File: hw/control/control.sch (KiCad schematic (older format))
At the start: 3 parts, among them J101 Screw_Terminal_01x02, J102 Screw_Terminal_01x03, J103 Screw_Terminal_01x03

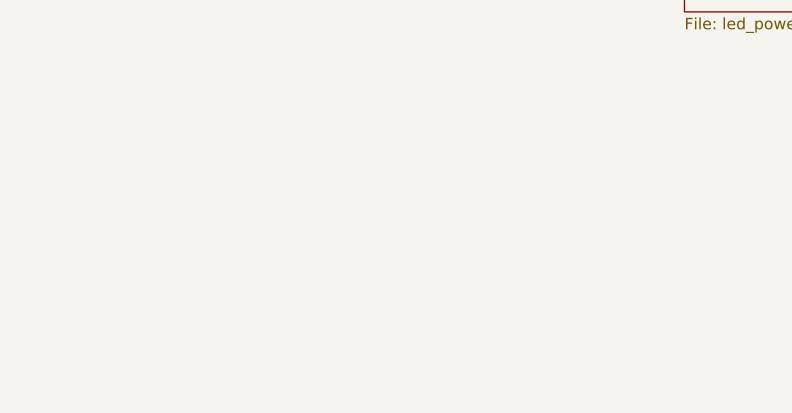
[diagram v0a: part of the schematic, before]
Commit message: [hw] Spread-out the components on control layout
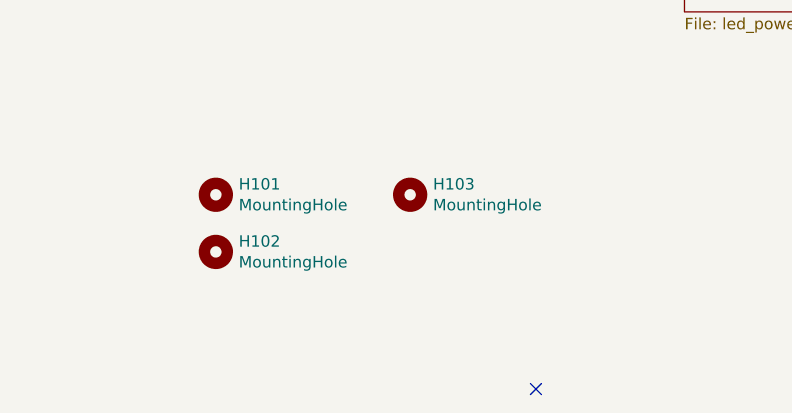
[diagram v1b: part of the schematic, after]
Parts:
- added H101, H102, H103: MountingHole, MountingHole:MountingHole_2.7mm_M2.5, symbol Mechanical:MountingHole
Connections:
- no-connect marks 0 -> 1
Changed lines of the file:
@@
 Wire Wire Line
 	3300 2550 3100 2550
+NoConn ~ 3200 7250
 Wire Bus Line
 	6350 3000 6350 4750
@@
 Wire Bus Line
 	6250 2750 6250 5050
+$Comp
+L Mechanical:MountingHole H101
+U 1 1 6167B012
+P 1800 6400
+F 0 "H101" H 1900 6446 50  0000 L CNN
+F 1 "MountingHole" H 1900 6355 50  0000 L CNN
+F 2 "MountingHole:MountingHole_2.7mm_M2.5" H 1800 6400 50  0001 C CNN
+F 3 "~" H 1800 6400 50  0001 C CNN
+	1    1800 6400
+	1    0    0    -1
+$EndComp
+$Comp
+L Mechanical:MountingHole H102
+U 1 1 6167B2FA
+P 1800 6650
+F 0 "H102" H 1900 6696 50  0000 L CNN
+F 1 "MountingHole" H 1900 6605 50  0000 L CNN
+F 2 "MountingHole:MountingHole_2.7mm_M2.5" H 1800 6650 50  0001 C CNN
+F 3 "~" H 1800 6650 50  0001 C CNN
+	1    1800 6650
+	1    0    0    -1
+$EndComp
+$Comp
+L Mechanical:MountingHole H103
+U 1 1 6167B527
+P 2650 6400
+F 0 "H103" H 2750 6446 50  0000 L CNN
+F 1 "MountingHole" H 2750 6355 50  0000 L CNN
+F 2 "MountingHole:MountingHole_2.7mm_M2.5" H 2650 6400 50  0001 C CNN
+F 3 "~" H 2650 6400 50  0001 C CNN
+	1    2650 6400
+	1    0    0    -1
+$EndComp
 $EndSCHEMATC

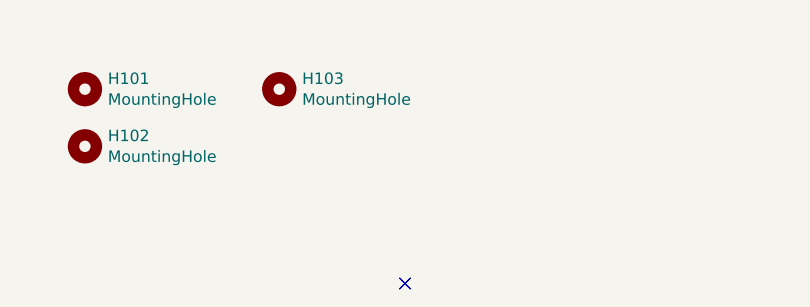
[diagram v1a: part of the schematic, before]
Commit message: [hw] Add control board net classes
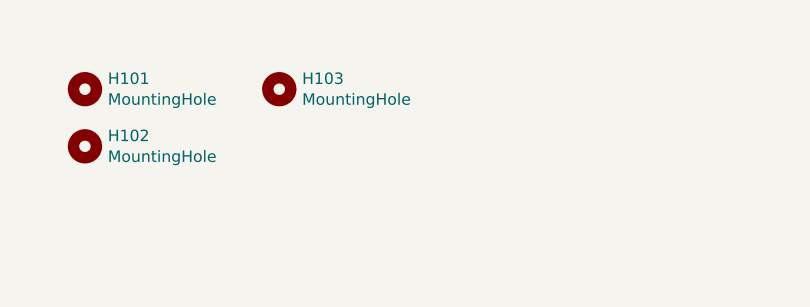
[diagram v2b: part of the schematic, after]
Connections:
- no-connect marks 1 -> 0
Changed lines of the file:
@@
 Wire Wire Line
 	3300 2550 3100 2550
-NoConn ~ 3200 7250
-Wire Bus Line
-	6350 3000 6350 4750
-Wire Bus Line
-	5950 2500 5950 5500
-Wire Bus Line
-	6250 2750 6250 5050
 $Comp
 L Mechanical:MountingHole H101
@@
 	1    0    0    -1
 $EndComp
+Wire Bus Line
+	6350 3000 6350 4750
+Wire Bus Line
+	5950 2500 5950 5500
+Wire Bus Line
+	6250 2750 6250 5050
 $EndSCHEMATC

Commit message: [hw] Incorporate suggestions
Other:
- moved on the sheet: J101, J103
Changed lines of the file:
@@
 L Connector:Screw_Terminal_01x03 J103
 U 1 1 614B768A
-P 9200 5100
-F 0 "J103" H 9350 5050 50  0000 C CNN
-F 1 "Screw_Terminal_01x03" H 9700 5200 50  0000 C CNN
-F 2 "TerminalBlock_Phoenix:TerminalBlock_Phoenix_MKDS-1,5-3_1x03_P5.00mm_Horizontal" H 9200 5100 50  0001 C CNN
-F 3 "~" H 9200 5100 50  0001 C CNN
-	1    9200 5100
-	1    0    0    1
+P 9200 5300
+F 0 "J103" H 9350 5250 50  0000 C CNN
+F 1 "Screw_Terminal_01x03" H 9700 5400 50  0000 C CNN
+F 2 "TerminalBlock_Phoenix:TerminalBlock_Phoenix_MKDS-1,5-3_1x03_P5.00mm_Horizontal" H 9200 5300 50  0001 C CNN
+F 3 "~" H 9200 5300 50  0001 C CNN
+	1    9200 5300
+	1    0    0    -1
 $EndComp
 $Comp
 L power:GND #PWR0103
 U 1 1 614C271E
-P 9650 4750
-F 0 "#PWR0103" H 9650 4500 50  0001 C CNN
-F 1 "GND" H 9655 4577 50  0000 C CNN
-F 2 "" H 9650 4750 50  0001 C CNN
-F 3 "" H 9650 4750 50  0001 C CNN
-	1    9650 4750
+P 9000 4600
+F 0 "#PWR0103" H 9000 4350 50  0001 C CNN
+F 1 "GND" H 9005 4427 50  0000 C CNN
+F 2 "" H 9000 4600 50  0001 C CNN
+F 3 "" H 9000 4600 50  0001 C CNN
+	1    9000 4600
 	1    0    0    -1
 $EndComp
@@
 Wire Wire Line
 	3650 3350 3650 2550
-Wire Wire Line
-	3650 2550 3300 2550
 Connection ~ 3650 3350
 Entry Wire Line
@@
 	5850 5450 5200 5450
 Wire Wire Line
-	9650 4750 9000 4750
-Wire Wire Line
-	9000 4750 9000 4500
-Wire Wire Line
-	9000 4750 9000 5000
-Connection ~ 9000 4750
+	9000 4600 9000 4500
 Wire Wire Line
 	8600 4650 8800 4650
@@
 	8600 4850 8800 4850
 Wire Wire Line
-	8800 4850 8800 5100
-Wire Wire Line
-	8800 5100 9000 5100
+	8800 4850 8800 5300
+Wire Wire Line
+	8800 5300 9000 5300
 Wire Wire Line
 	5200 5200 9000 5200
@@
 L Connector:Screw_Terminal_01x02 J101
 U 1 1 615338F7
-P 1350 2600
-F 0 "J101" H 1268 2817 50  0000 C CNN
-F 1 "Screw_Terminal_01x02" H 1268 2726 50  0000 C CNN
-F 2 "TerminalBlock_Phoenix:TerminalBlock_Phoenix_MKDS-1,5-2_1x02_P5.00mm_Horizontal" H 1350 2600 50  0001 C CNN
-F 3 "~" H 1350 2600 50  0001 C CNN
-	1    1350 2600
+P 1000 2600
+F 0 "J101" H 918 2817 50  0000 C CNN
+F 1 "Screw_Terminal_01x02" H 918 2726 50  0000 C CNN
+F 2 "TerminalBlock_Phoenix:TerminalBlock_Phoenix_MKDS-1,5-2_1x02_P5.00mm_Horizontal" H 1000 2600 50  0001 C CNN
+F 3 "~" H 1000 2600 50  0001 C CNN
+	1    1000 2600
 	-1   0    0    -1
 $EndComp
 Wire Wire Line
-	1650 2550 1650 2600
-Wire Wire Line
-	1650 2600 1550 2600
-Wire Wire Line
-	1650 2750 1650 2700
-Wire Wire Line
-	1650 2700 1550 2700
+	1450 2550 1450 2600
+Wire Wire Line
+	1450 2600 1200 2600
+Wire Wire Line
+	1450 2750 1450 2700
+Wire Wire Line
+	1450 2700 1200 2700
 Wire Wire Line
 	5650 3350 5650 3200
@@
 P 5400 3350
 F 0 "#FLG0103" H 5400 3425 50  0001 C CNN
-F 1 "PWR_FLAG" H 5400 3523 50  0000 C CNN
+F 1 "PWR_FLAG" H 5400 3500 50  0000 C CNN
 F 2 "" H 5400 3350 50  0001 C CNN
 F 3 "~" H 5400 3350 50  0001 C CNN
@@
 Wire Wire Line
 	5400 3350 5650 3350
-$Comp
-L power:PWR_FLAG #FLG0102
-U 1 1 61668437
-P 3300 2750
-F 0 "#FLG0102" H 3300 2825 50  0001 C CNN
-F 1 "PWR_FLAG" H 3300 2900 50  0000 C CNN
-F 2 "" H 3300 2750 50  0001 C CNN
-F 3 "~" H 3300 2750 50  0001 C CNN
-	1    3300 2750
-	1    0    0    -1
-$EndComp
-Connection ~ 3300 2750
-Wire Wire Line
-	1650 2750 2000 2750
-Wire Wire Line
-	1650 2550 2000 2550
-$Comp
-L power:PWR_FLAG #FLG0101
-U 1 1 6166B01E
-P 3300 2550
-F 0 "#FLG0101" H 3300 2625 50  0001 C CNN
-F 1 "PWR_FLAG" H 3300 2723 50  0000 C CNN
-F 2 "" H 3300 2550 50  0001 C CNN
-F 3 "~" H 3300 2550 50  0001 C CNN
-	1    3300 2550
-	1    0    0    -1
-$EndComp
-Connection ~ 3300 2550
-Wire Wire Line
-	3300 2550 3100 2550
+Wire Wire Line
+	1450 2750 1750 2750
+Wire Wire Line
+	1450 2550 1750 2550
 $Comp
 L Mechanical:MountingHole H101
@@
 	1    0    0    -1
 $EndComp
+$Comp
+L power:GND #PWR0104
+U 1 1 6169E8B0
+P 9000 5500
+F 0 "#PWR0104" H 9000 5250 50  0001 C CNN
+F 1 "GND" H 9005 5327 50  0000 C CNN
+F 2 "" H 9000 5500 50  0001 C CNN
+F 3 "" H 9000 5500 50  0001 C CNN
+	1    9000 5500
+	1    0    0    -1
+$EndComp
+Wire Wire Line
+	9000 5500 9000 5400
+$Comp
+L power:PWR_FLAG #FLG0101
+U 1 1 616A47D9
+P 1750 2550
+F 0 "#FLG0101" H 1750 2625 50  0001 C CNN
+F 1 "PWR_FLAG" H 1750 2700 50  0000 C CNN
+F 2 "" H 1750 2550 50  0001 C CNN
+F 3 "~" H 1750 2550 50  0001 C CNN
+	1    1750 2550
+	1    0    0    -1
+$EndComp
+Connection ~ 1750 2550
+Wire Wire Line
+	1750 2550 2000 2550
+$Comp
+L power:PWR_FLAG #FLG0102
+U 1 1 616A4B57
+P 1750 2750
+F 0 "#FLG0102" H 1750 2825 50  0001 C CNN
+F 1 "PWR_FLAG" H 1750 2900 50  0000 C CNN
+F 2 "" H 1750 2750 50  0001 C CNN
+F 3 "~" H 1750 2750 50  0001 C CNN
+	1    1750 2750
+	1    0    0    -1
+$EndComp
+Connection ~ 1750 2750
+Wire Wire Line
+	1750 2750 2000 2750
+Wire Wire Line
+	3100 2550 3500 2550
+$Comp
+L power:PWR_FLAG #FLG0104
+U 1 1 616A5315
+P 3500 2550
+F 0 "#FLG0104" H 3500 2625 50  0001 C CNN
+F 1 "PWR_FLAG" H 3500 2700 50  0000 C CNN
+F 2 "" H 3500 2550 50  0001 C CNN
+F 3 "~" H 3500 2550 50  0001 C CNN
+	1    3500 2550
+	1    0    0    -1
+$EndComp
+Connection ~ 3500 2550
+Wire Wire Line
+	3500 2550 3650 2550
 Wire Bus Line
 	6350 3000 6350 4750

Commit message: [hw] Re-annotate all components
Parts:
- renumbered H103 to H102, H102 to H103
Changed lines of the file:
@@
 LED_DATA_~EN~1
 $Comp
-L power:PWR_FLAG #FLG0103
+L power:PWR_FLAG #FLG0104
 U 1 1 61664238
 P 5400 3350
-F 0 "#FLG0103" H 5400 3425 50  0001 C CNN
+F 0 "#FLG0104" H 5400 3425 50  0001 C CNN
 F 1 "PWR_FLAG" H 5400 3500 50  0000 C CNN
 F 2 "" H 5400 3350 50  0001 C CNN
@@
 $EndComp
 $Comp
-L Mechanical:MountingHole H102
+L Mechanical:MountingHole H103
 U 1 1 6167B2FA
 P 1800 6650
-F 0 "H102" H 1900 6696 50  0000 L CNN
+F 0 "H103" H 1900 6696 50  0000 L CNN
 F 1 "MountingHole" H 1900 6605 50  0000 L CNN
 F 2 "MountingHole:MountingHole_2.7mm_M2.5" H 1800 6650 50  0001 C CNN
@@
 $EndComp
 $Comp
-L Mechanical:MountingHole H103
+L Mechanical:MountingHole H102
 U 1 1 6167B527
 P 2650 6400
-F 0 "H103" H 2750 6446 50  0000 L CNN
+F 0 "H102" H 2750 6446 50  0000 L CNN
 F 1 "MountingHole" H 2750 6355 50  0000 L CNN
 F 2 "MountingHole:MountingHole_2.7mm_M2.5" H 2650 6400 50  0001 C CNN
@@
 	1750 2550 2000 2550
 $Comp
-L power:PWR_FLAG #FLG0102
+L power:PWR_FLAG #FLG0103
 U 1 1 616A4B57
 P 1750 2750
-F 0 "#FLG0102" H 1750 2825 50  0001 C CNN
+F 0 "#FLG0103" H 1750 2825 50  0001 C CNN
 F 1 "PWR_FLAG" H 1750 2900 50  0000 C CNN
 F 2 "" H 1750 2750 50  0001 C CNN
@@
 	3100 2550 3500 2550
 $Comp
-L power:PWR_FLAG #FLG0104
+L power:PWR_FLAG #FLG0102
 U 1 1 616A5315
 P 3500 2550
-F 0 "#FLG0104" H 3500 2625 50  0001 C CNN
+F 0 "#FLG0102" H 3500 2625 50  0001 C CNN
 F 1 "PWR_FLAG" H 3500 2700 50  0000 C CNN
 F 2 "" H 3500 2550 50  0001 C CNN
